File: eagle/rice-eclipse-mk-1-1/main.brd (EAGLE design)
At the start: 110.2 x 91.2 mm, 136 parts, among them IC1 LMV321LICTRT, IC2 LMV321LICTRT, IC3 LMV321LICTRT, IC4 LMV321LICTRT, IC5 UA78M, IC6 LMV321LICTRT, IC7 LMV321LICTRT, IC8 LMV321LICTRT, IC9 LMV321LICTRT, U1 LM1084ISX-5.0/NOPB, U2 THS4531IDRD8-M, U3 THS4531IDRD8-M, U4 THS4531IDRD8-M, U5 THS4531IDRD8-M, U6 1101M2S3CQE2

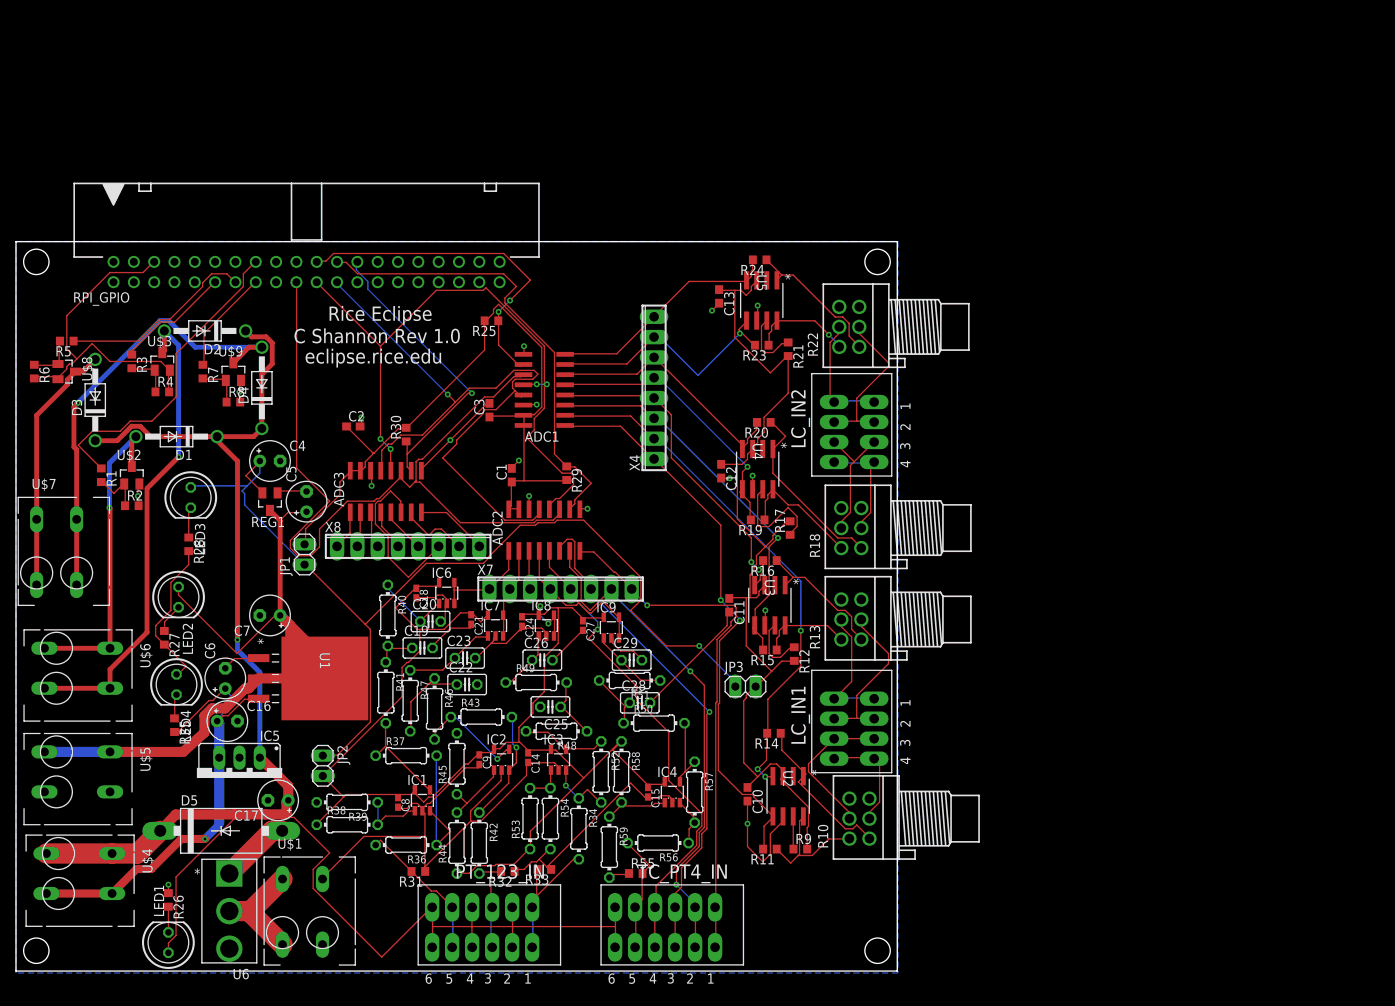
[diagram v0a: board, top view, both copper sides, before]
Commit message: Removed all vias that were too small. Ready2Route.
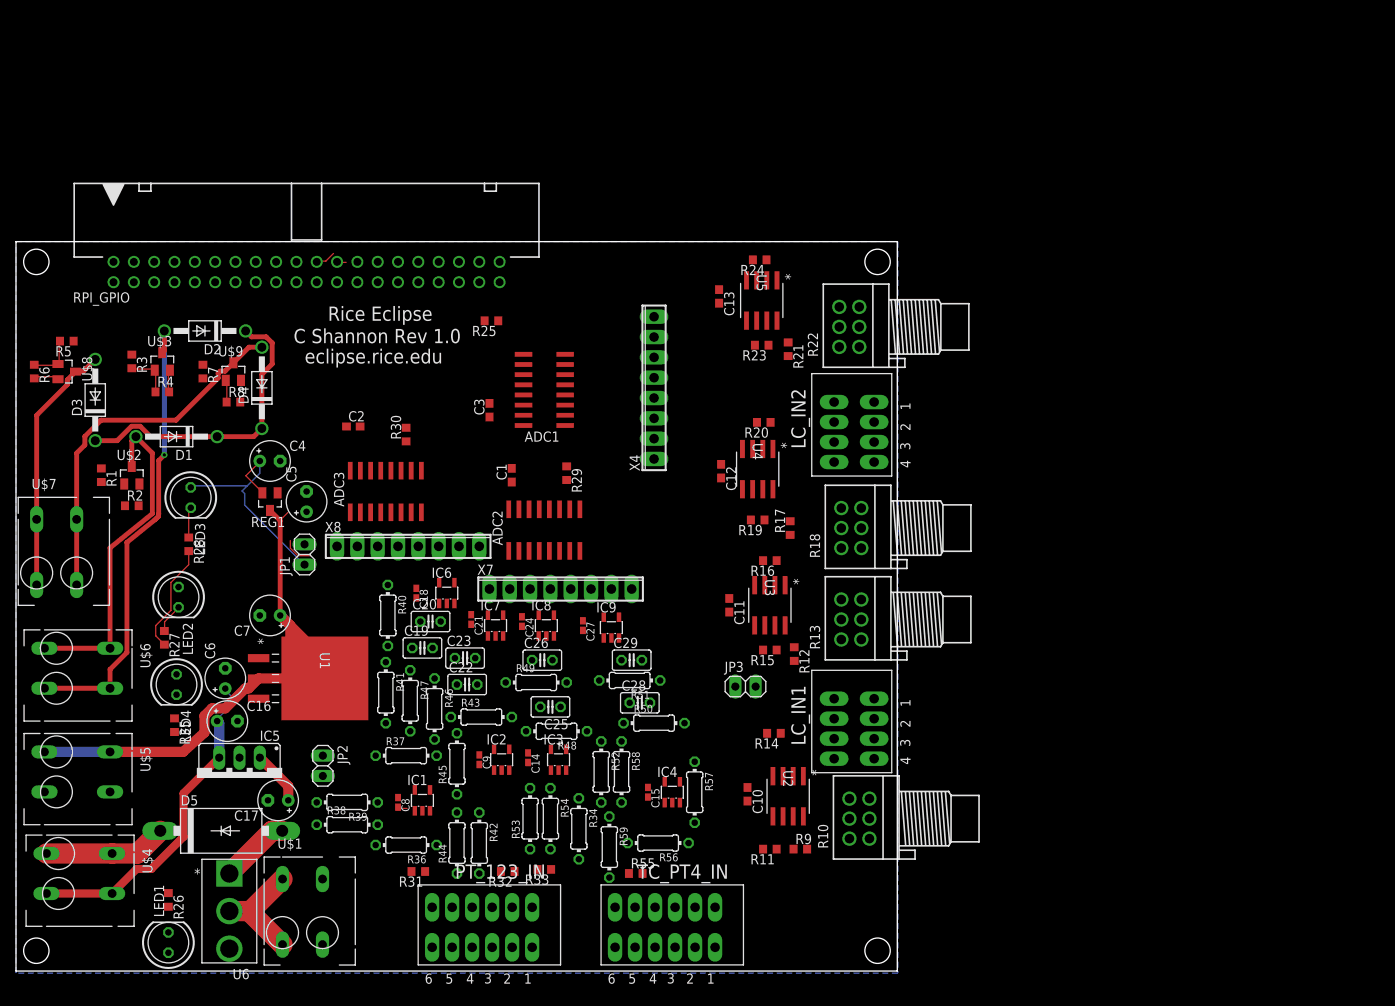
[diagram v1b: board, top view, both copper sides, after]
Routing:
- net GND: track 276.6 -> 21.4 mm, vias 17 -> 0
- net +3V3_PT: track 161.6 -> 0.39 mm
- net +12V: track 218.4 -> 60.2 mm, vias 1 -> 0
- net +3V3_LC: track 116.3 -> 0.00 mm
- net MOSI: track 102.6 -> 3.89 mm
- net +3V3: track 125.7 -> 30.1 mm, vias 1 -> 0
- net +3V3_ADC: track 88.8 -> 0.00 mm
- net MISO: track 83.1 -> 0.00 mm, vias 4 -> 0
- net SCLK: track 83.1 -> 0.00 mm, vias 1 -> 0
- net ADC1_A0: track 71.4 -> 0.00 mm, vias 2 -> 0
- net ADC2_A7: track 66.3 -> 0.00 mm, vias 1 -> 0
- net ADC1_A1: track 66.2 -> 0.00 mm, vias 3 -> 0
- net ADC2_A6: track 64.3 -> 0.00 mm, vias 2 -> 0
- net ADC2_A5: track 62.7 -> 0.00 mm, vias 1 -> 0
- net ADC2_A4: track 60.8 -> 0.00 mm, vias 1 -> 0
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
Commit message: Moved all the stuff again.
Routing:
- net SOLENOID_1_NEGATIVE: track 58.7 -> 96.1 mm, vias 1 -> 0
- net +12V: track 60.2 -> 88.4 mm, vias 0 -> 1
- net +3V3: track 30.1 -> 4.11 mm
- net GND: track 21.4 -> 39.2 mm
- net RELAY_NEGATIVE: track 42.0 -> 30.7 mm
- net N$7: track 6.23 -> 0.00 mm
- net N$6: track 5.86 -> 0.00 mm
- net +5V: track 68.8 -> 72.8 mm
- net MOSI: track 3.89 -> 0.00 mm
- net N$3: track 3.82 -> 0.00 mm
- net N$2: track 3.69 -> 0.00 mm
- net +10V: track 42.1 -> 45.6 mm
- net N$8: track 2.85 -> 0.00 mm
- net ADC1_CS: track 2.56 -> 0.00 mm
- net SOLENOID_3_NEGATIVE: track 46.2 -> 43.8 mm
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
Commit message: Added some stuff.
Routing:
- net GND: track 39.2 -> 363.2 mm, vias 0 -> 14
- net +3V3_PT: track 0.00 -> 191.1 mm
- net +12V: track 88.4 -> 226.6 mm
- net +3V3_LC: track 0.00 -> 131.2 mm
- net +3V3: track 4.11 -> 121.7 mm, vias 0 -> 1
- net +3V3_ADC: track 0.00 -> 86.6 mm
- net ADC1_A0: track 0.00 -> 75.9 mm, vias 0 -> 1
- net MOSI: track 0.00 -> 75.9 mm, vias 0 -> 2
- net SCLK: track 0.00 -> 74.3 mm, vias 0 -> 4
- net MISO: track 0.00 -> 70.5 mm, vias 0 -> 2
- net ADC1_A1: track 0.00 -> 67.1 mm, vias 0 -> 1
- net ADC2_A7: track 0.00 -> 58.6 mm
- net ADC2_A6: track 0.00 -> 57.6 mm
- net ADC2_A5: track 0.00 -> 56.3 mm
- net ADC2_A4: track 0.00 -> 55.3 mm
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
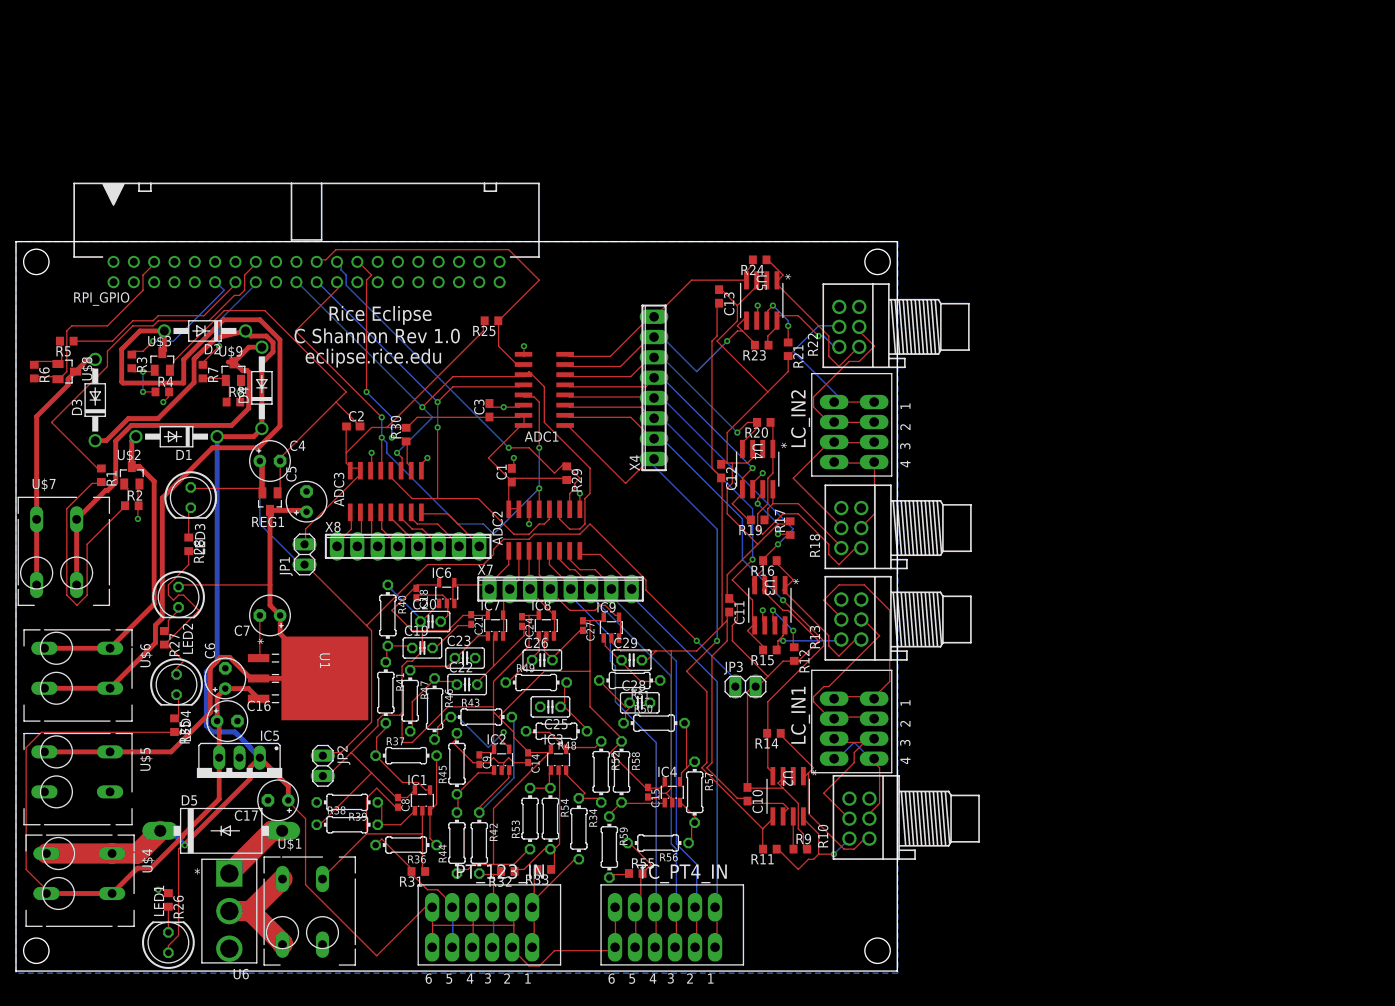
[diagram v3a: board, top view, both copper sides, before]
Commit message: Resized board and ready to reroute.
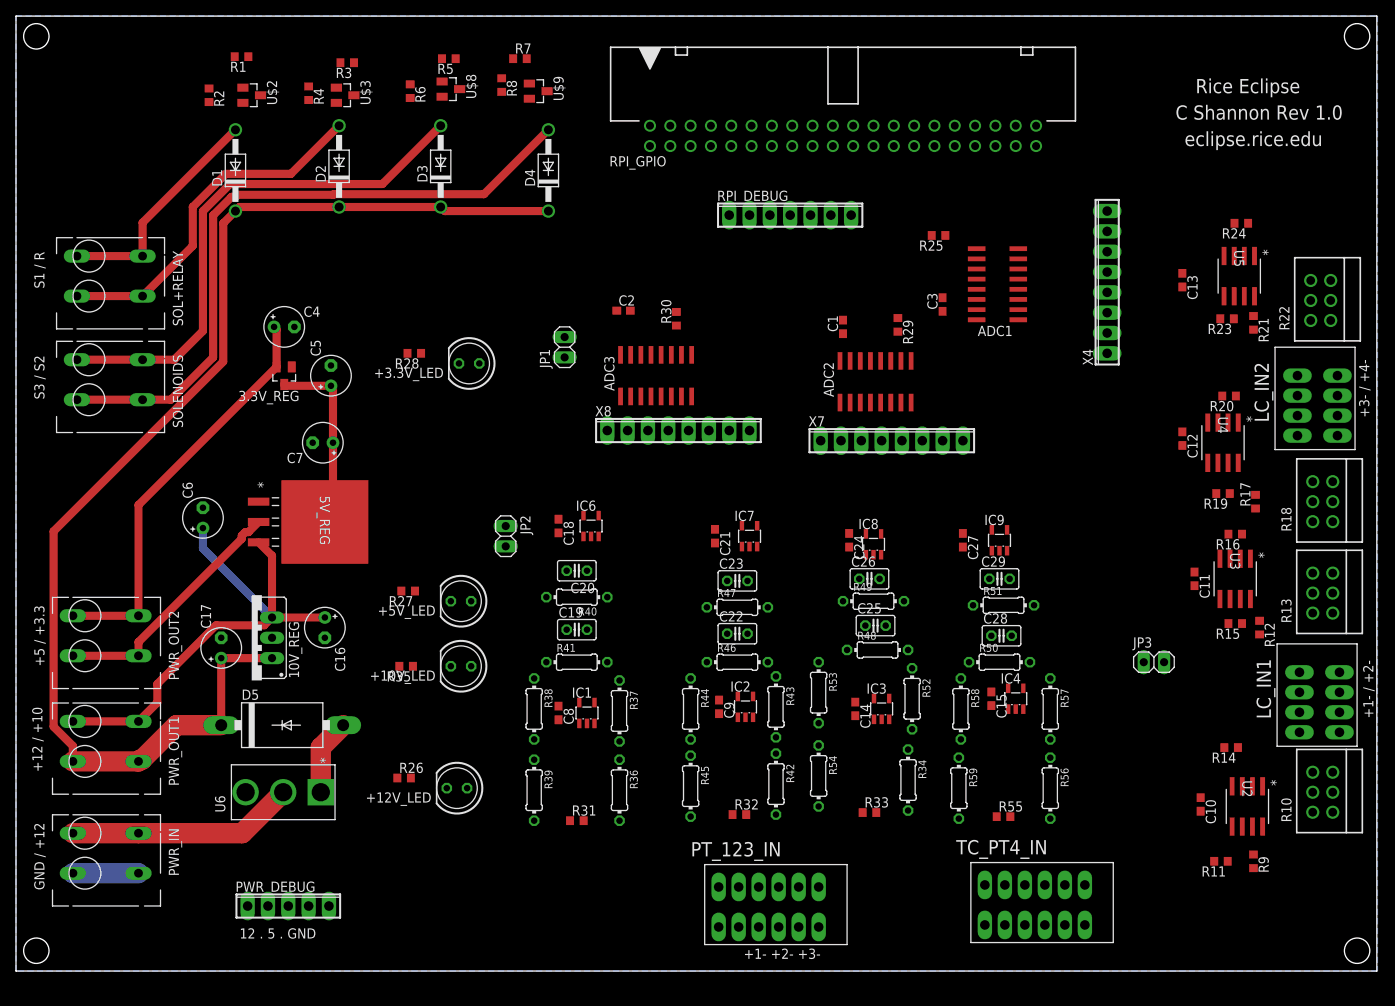
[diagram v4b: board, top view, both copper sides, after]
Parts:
- removed IC5: UA78M, texas-extra:TO220S
- removed LED1, LED2, LED3, LED4: (no value), led:LED5MM
- removed REG1: AP2210N-3.3TRG1, diodes-extra:SOT23
- removed U$1, U$4, U$5, U$6, U$7: 1991095, con-phoenix-500-extra:1991095
- removed U1: LM1084ISX-5.0/NOPB, texas-extra:TS3B
- added +10V_LED, +12V_LED, +3.3V_LED, +5V_LED: (no value), led:LED5MM
- added 10V_REG: UA78M, texas-extra:TO220S
- added 3.3V_REG: AP2210N-3.3TRG1, diodes-extra:SOT23
- added 5V_REG: LM1084ISX-5.0/NOPB, texas-extra:TS3B
- added PWR_DEBUG: (no value), con-phoenix-254:5POL254
- added PWR_IN, PWR_OUT1, PWR_OUT2, SOL+RELAY, SOLENOIDS: 1991095, con-phoenix-500-extra:1991095
- added RPI_DEBUG: (no value), con-phoenix-254:7POL254
- C14, C15, C18, C21, C24, C27, C8, C9: value 10nF -> 0.1UF; device rcl:C0402K -> rcl:C0603
- moved RPI_GPIO 69.2 mm to (103.4, 104.4)
- moved R24 60.4 mm to (153.2, 93.5)
- moved U5 59.8 mm to (152.9, 86.9)
- moved U$8 59.6 mm to (54.4, 110.2)
- moved R5 59.4 mm to (54.1, 114.0)
- moved R13 59.0 mm to (164.6, 47.2)
- moved R18 59.0 mm to (164.6, 58.7)
- moved R22 59.0 mm to (164.3, 83.8)
- moved R6 58.6 mm to (49.3, 110.0)
- moved LC_IN1 58.3 mm to (157.7, 40.9)
- moved R12 58.3 mm to (155.4, 42.9)
- moved R15 58.3 mm to (152.4, 43.4)
- moved R16 58.3 mm to (152.4, 54.6)
- moved R19 58.3 mm to (150.9, 59.7)
- moved R20 58.3 mm to (151.6, 71.9)
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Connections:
- net +10V: now also 10V_REG.3, 5V_REG.3, PWR_DEBUG.2, PWR_OUT1.A1, PWR_OUT1.B1; no longer IC5.3, U$4.A2, U$4.B2, U1.3
- net +12V: now also +12V_LED.A, 10V_REG.1, PWR_DEBUG.1, PWR_OUT1.A2, PWR_OUT1.B2; no longer IC5.1, LED1.A, U$4.A1, U$4.B1
- net +12V_DEBUG: now also PWR_IN.A1, PWR_IN.B1; no longer U$1.A1, U$1.B1
- net +3V3: now also +3.3V_LED.A, 3.3V_REG.2, PWR_DEBUG.4, PWR_OUT2.A1, PWR_OUT2.B1; no longer LED3.A, REG1.2
- net +5V: now also +5V_LED.A, 3.3V_REG.3, 5V_REG.2, 5V_REG.4, PWR_DEBUG.3, PWR_OUT2.A2, PWR_OUT2.B2; no longer LED2.A, REG1.3, U$5.A1, U$5.B1, U1.2, U1.4
- net ADC1_CS: now also RPI_DEBUG.4
- net ADC2_CS: now also RPI_DEBUG.3
- net ADC3_CS: now also RPI_DEBUG.2
- net GND: now also +10V_LED.K, 10V_REG.2, 3.3V_REG.1, 5V_REG.1, PWR_DEBUG.5, PWR_IN.A2, PWR_IN.B2, RPI_DEBUG.1; no longer IC5.2, LED4.A, REG1.1, U$1.A2, U$1.B2, U$5.A2, U$5.B2, U1.1
- net MISO: now also RPI_DEBUG.6
- net MOSI: now also RPI_DEBUG.5
- net N$1: now also +12V_LED.K; no longer LED1.K
- net N$2: now also +5V_LED.K; no longer LED2.K
- net N$3: now also +3.3V_LED.K; no longer LED3.K
- net N$9: now also +10V_LED.A; no longer LED4.K
- net RELAY_NEGATIVE: now also SOL+RELAY.A1, SOL+RELAY.B1; no longer U$6.A1, U$6.B1
- net SCLK: now also RPI_DEBUG.7
- net SOLENOID_1_NEGATIVE: now also SOL+RELAY.A2, SOL+RELAY.B2; no longer U$6.A2, U$6.B2
- net SOLENOID_2_NEGATIVE: now also SOLENOIDS.A1, SOLENOIDS.B1; no longer U$7.A1, U$7.B1
- net SOLENOID_3_NEGATIVE: now also SOLENOIDS.A2, SOLENOIDS.B2; no longer U$7.A2, U$7.B2
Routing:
- net GND: track 363.2 -> 8.20 mm, vias 14 -> 0
- net +3V3_PT: track 191.1 -> 0.00 mm
- net +3V3_LC: track 131.2 -> 0.00 mm
- net +3V3_ADC: track 86.6 -> 0.00 mm
- net ADC1_A0: track 75.9 -> 0.00 mm, vias 1 -> 0
- net MOSI: track 75.9 -> 0.00 mm, vias 2 -> 0
- net SCLK: track 74.3 -> 0.00 mm, vias 4 -> 0
- net +12V: track 226.6 -> 153.9 mm, vias 1 -> 0
- net MISO: track 70.5 -> 0.00 mm, vias 2 -> 0
- net +3V3: track 121.7 -> 51.6 mm, vias 1 -> 0
- net ADC1_A1: track 67.1 -> 0.00 mm, vias 1 -> 0
- net ADC2_A7: track 58.6 -> 0.00 mm
- net SOLENOID_1_NEGATIVE: track 103.0 -> 44.4 mm
- net ADC2_A6: track 57.6 -> 0.00 mm
- net ADC2_A5: track 56.3 -> 0.00 mm
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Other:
- board size 110.2 x 91.2 mm -> 170.1 x 119.4 mm
